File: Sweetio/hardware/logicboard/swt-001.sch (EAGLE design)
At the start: 44 parts, among them IC1 74ACT06N, J1 MKR, J10 THS, J16 MNTR, J2 GPIO, J5 SPI, J6 LED, J7 DIN5, J8 DIN5, J9 DIN5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

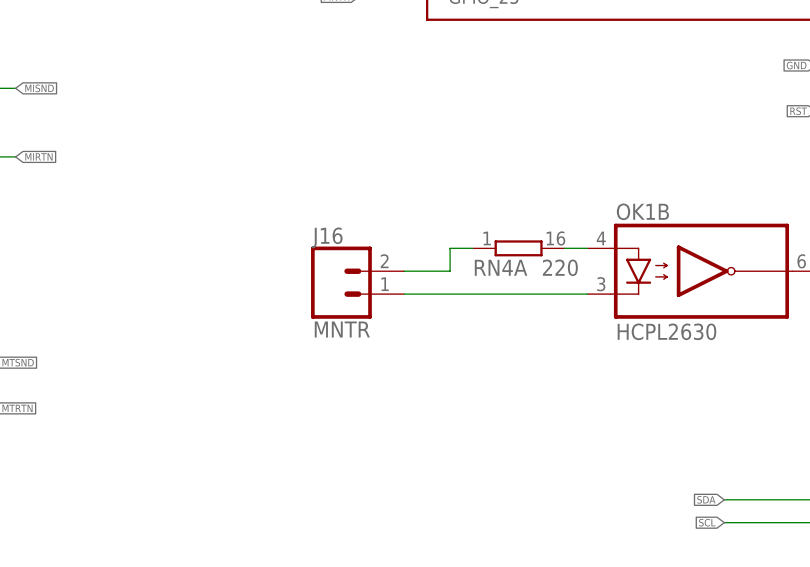
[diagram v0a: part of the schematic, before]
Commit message: Moved JP00.
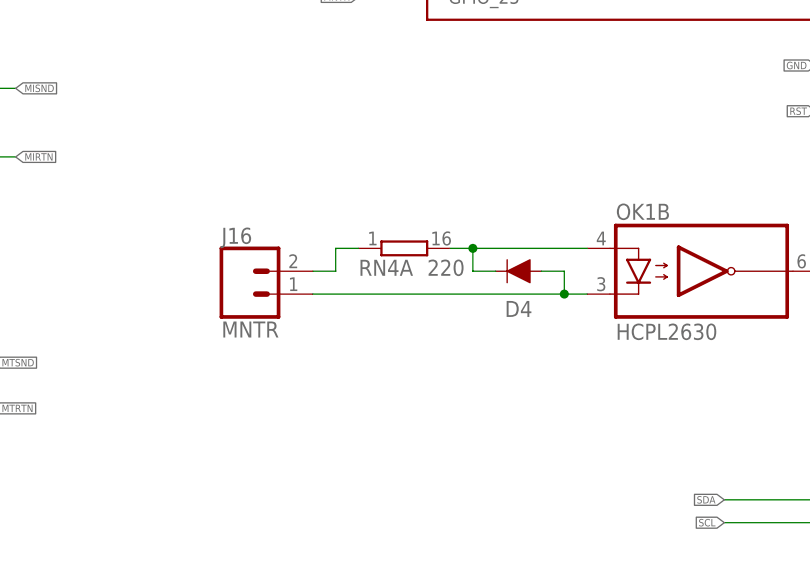
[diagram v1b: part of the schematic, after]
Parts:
- added D4: DIODE-1N4148, SparkFun-DiscreteSemi:DIODE-1N4148
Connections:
- net N$2 renamed BASE
- net N$3 renamed COLLECTOR
- net SND renamed MNTRA
- removed net N$1: OK1B.A2, RN4A.2
- removed net RTN: J16.1, OK1B.C2
- new net MNTRAA: D4.C, OK1B.A2, RN4A.2
- new net MNTRK: D4.A, J16.1, OK1B.C2
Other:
- moved on the sheet: J16, RN4A
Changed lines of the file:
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@@
 <part name="J21" library="Connector" deviceset="TWIG-4P-2.0" device=""/>
 <part name="J22" library="Connector" deviceset="TWIG-4P-2.0" device=""/>
+<part name="D4" library="SparkFun-DiscreteSemi" library_urn="urn:adsk.eagle:library:514" deviceset="DIODE" device="-1N4148" package3d_urn="urn:adsk.eagle:package:38452/1" value=""/>
 </parts>
 <sheets>
@@
 <instance part="NC1" gate="G$1" x="302.26" y="177.8" smashed="yes"/>
 <instance part="NC2" gate="G$1" x="302.26" y="175.26" smashed="yes"/>
-<instance part="RN4" gate="A" x="243.84" y="106.68" smashed="yes">
-<attribute name="VALUE" x="246.38" y="103.632" size="1.778" layer="96"/>
-<attribute name="NAME" x="238.76" y="103.632" size="1.778" layer="95"/>
+<instance part="RN4" gate="A" x="231.14" y="106.68" smashed="yes">
+<attribute name="VALUE" x="233.68" y="103.632" size="1.778" layer="96"/>
+<attribute name="NAME" x="226.06" y="103.632" size="1.778" layer="95"/>
 </instance>
 <instance part="RN4" gate="B" x="177.8" y="124.46" smashed="yes">
@@
 <attribute name="VALUE" x="288.29" y="116.84" size="1.778" layer="96"/>
 </instance>
-<instance part="J16" gate="J1" x="223.52" y="101.6" smashed="yes">
-<attribute name="VALUE" x="220.98" y="96.774" size="1.778" layer="96" font="vector"/>
-<attribute name="NAME" x="220.98" y="107.188" size="1.778" layer="95" font="vector"/>
+<instance part="J16" gate="J1" x="213.36" y="101.6" smashed="yes">
+<attribute name="VALUE" x="210.82" y="96.774" size="1.778" layer="96" font="vector"/>
+<attribute name="NAME" x="210.82" y="107.188" size="1.778" layer="95" font="vector"/>
 </instance>
 <instance part="JP2" gate="J1" x="50.8" y="111.76" smashed="yes">
@@
 <attribute name="NAME" x="77.47" y="86.36" size="1.27" layer="95" rot="R180"/>
 <attribute name="VALUE" x="73.66" y="95.25" size="1.27" layer="96" rot="R270"/>
+</instance>
+<instance part="D4" gate="G$1" x="243.84" y="104.14" smashed="yes" rot="R180">
+<attribute name="NAME" x="243.84" y="99.06" size="1.778" layer="95" align="bottom-center"/>
+<attribute name="VALUE" x="246.38" y="106.172" size="1.778" layer="96" font="vector" rot="R180" align="top-left"/>
 </instance>
 </instances>
@@
 </segment>
 </net>
-<net name="N$1" class="1">
+<net name="MNTRAA" class="1">
 <segment>
 <pinref part="OK1" gate="B" pin="A2"/>
-<wire x1="251.46" y1="106.68" x2="248.92" y2="106.68" width="0.1524" layer="91"/>
+<wire x1="251.46" y1="106.68" x2="238.76" y2="106.68" width="0.1524" layer="91"/>
 <pinref part="RN4" gate="A" pin="2"/>
-</segment>
-</net>
-<net name="RTN" class="1">
+<pinref part="D4" gate="G$1" pin="C"/>
+<wire x1="238.76" y1="106.68" x2="236.22" y2="106.68" width="0.1524" layer="91"/>
+<wire x1="241.3" y1="104.14" x2="238.76" y2="104.14" width="0.1524" layer="91"/>
+<wire x1="238.76" y1="104.14" x2="238.76" y2="106.68" width="0.1524" layer="91"/>
+<junction x="238.76" y="106.68"/>
+</segment>
+</net>
+<net name="MNTRK" class="1">
 <segment>
 <pinref part="OK1" gate="B" pin="C2"/>
-<wire x1="251.46" y1="101.6" x2="231.14" y2="101.6" width="0.1524" layer="91"/>
+<wire x1="251.46" y1="101.6" x2="248.92" y2="101.6" width="0.1524" layer="91"/>
 <pinref part="J16" gate="J1" pin="1"/>
-</segment>
-</net>
-<net name="SND" class="0">
+<pinref part="D4" gate="G$1" pin="A"/>
+<wire x1="248.92" y1="101.6" x2="220.98" y2="101.6" width="0.1524" layer="91"/>
+<wire x1="246.38" y1="104.14" x2="248.92" y2="104.14" width="0.1524" layer="91"/>
+<wire x1="248.92" y1="104.14" x2="248.92" y2="101.6" width="0.1524" layer="91"/>
+<junction x="248.92" y="101.6"/>
+</segment>
+</net>
+<net name="MNTRA" class="0">
 <segment>
 <pinref part="RN4" gate="A" pin="1"/>
-<wire x1="238.76" y1="106.68" x2="236.22" y2="106.68" width="0.1524" layer="91"/>
-<wire x1="236.22" y1="106.68" x2="236.22" y2="104.14" width="0.1524" layer="91"/>
+<wire x1="226.06" y1="106.68" x2="223.52" y2="106.68" width="0.1524" layer="91"/>
+<wire x1="223.52" y1="106.68" x2="223.52" y2="104.14" width="0.1524" layer="91"/>
 <pinref part="J16" gate="J1" pin="2"/>
-<wire x1="236.22" y1="104.14" x2="231.14" y2="104.14" width="0.1524" layer="91"/>
+<wire x1="223.52" y1="104.14" x2="220.98" y2="104.14" width="0.1524" layer="91"/>
 </segment>
 </net>
@@
 </segment>
 </net>
-<net name="N$2" class="0">
+<net name="BASE" class="0">
 <segment>
 <pinref part="T1" gate="G$1" pin="B"/>
@@
 </segment>
 </net>
-<net name="N$3" class="0">
+<net name="COLLECTOR" class="0">
 <segment>
 <pinref part="T1" gate="G$1" pin="C"/>

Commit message: RST switch.
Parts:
- removed JP6: LED, pinhead:PINHD-1X3
- added LED0, LED1: (no value), led:LEDCHIPLED_0603
- added S1: (no value), switch-omron:31-XX
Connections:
- net GND: now also LED0.C, LED1.C, S1.P; no longer JP6.2
- net LED0A: now also LED0.A; no longer JP6.3
- net LED1A: now also LED1.A; no longer JP6.1
- net RST: now also S1.S
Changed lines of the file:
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@@
 <part name="R4" library="resistor" library_urn="urn:adsk.eagle:library:348" deviceset="R-EU_" device="0204/5" package3d_urn="urn:adsk.eagle:package:23488/1" value="1k"/>
 <part name="R5" library="resistor" library_urn="urn:adsk.eagle:library:348" deviceset="R-EU_" device="0204/5" package3d_urn="urn:adsk.eagle:package:23488/1" value="1k"/>
-<part name="JP6" library="pinhead" library_urn="urn:adsk.eagle:library:325" deviceset="PINHD-1X3" device="" package3d_urn="urn:adsk.eagle:package:22458/2" value="LED"/>
 <part name="SUPPLY3" library="supply2" deviceset="GND" device=""/>
 <part name="C6" library="resistor" library_urn="urn:adsk.eagle:library:348" deviceset="C-EU" device="025-024X044" package3d_urn="urn:adsk.eagle:package:23630/1" value="10n"/>
@@
 <part name="J22" library="Connector" deviceset="TWIG-4P-2.0" device=""/>
 <part name="D4" library="SparkFun-DiscreteSemi" library_urn="urn:adsk.eagle:library:514" deviceset="DIODE" device="-1N4148" package3d_urn="urn:adsk.eagle:package:38452/1" value=""/>
+<part name="LED1" library="led" library_urn="urn:adsk.eagle:library:259" deviceset="LED" device="CHIPLED_0603" package3d_urn="urn:adsk.eagle:package:15822/2"/>
+<part name="LED0" library="led" library_urn="urn:adsk.eagle:library:259" deviceset="LED" device="CHIPLED_0603" package3d_urn="urn:adsk.eagle:package:15822/2"/>
+<part name="SUPPLY12" library="supply2" deviceset="GND" device=""/>
+<part name="S1" library="switch-omron" library_urn="urn:adsk.eagle:library:377" deviceset="31-XX" device="" package3d_urn="urn:adsk.eagle:package:27487/1"/>
 </parts>
 <sheets>
@@
 <attribute name="VALUE" x="93.98" y="35.56" size="1.778" layer="96" align="top-center"/>
 </instance>
-<instance part="JP6" gate="A" x="63.5" y="35.56" smashed="yes" rot="MR0">
-<attribute name="NAME" x="69.85" y="41.275" size="1.778" layer="95" rot="MR0"/>
-<attribute name="VALUE" x="69.85" y="27.94" size="1.778" layer="96" rot="MR0"/>
-</instance>
 <instance part="SUPPLY3" gate="GND" x="276.86" y="198.12" smashed="yes"/>
 <instance part="C6" gate="G$1" x="276.86" y="213.36" smashed="yes">
@@
 <attribute name="VALUE" x="246.38" y="106.172" size="1.778" layer="96" font="vector" rot="R180" align="top-left"/>
 </instance>
+<instance part="LED1" gate="G$1" x="68.58" y="38.1" smashed="yes" rot="R270">
+<attribute name="NAME" x="64.008" y="34.544" size="1.778" layer="95"/>
+<attribute name="VALUE" x="64.008" y="32.385" size="1.778" layer="96"/>
+</instance>
+<instance part="LED0" gate="G$1" x="68.58" y="33.02" smashed="yes" rot="R270">
+<attribute name="NAME" x="64.008" y="29.464" size="1.778" layer="95"/>
+<attribute name="VALUE" x="64.008" y="27.305" size="1.778" layer="96"/>
+</instance>
+<instance part="SUPPLY12" gate="GND" x="60.96" y="27.94" smashed="yes"/>
+<instance part="S1" gate="1" x="276.86" y="114.3" smashed="yes" rot="R270">
+<attribute name="NAME" x="274.955" y="120.65" size="1.778" layer="95"/>
+<attribute name="VALUE" x="280.035" y="118.11" size="1.778" layer="96"/>
+</instance>
 </instances>
 <busses>
@@
 <segment>
 <label x="101.6" y="35.56" size="0.8128" layer="95" xref="yes"/>
-<wire x1="66.04" y1="35.56" x2="78.74" y2="35.56" width="0.1524" layer="91"/>
-<pinref part="JP6" gate="A" pin="2"/>
 <pinref part="J6" gate="J$1" pin="2"/>
 <wire x1="78.74" y1="35.56" x2="101.6" y2="35.56" width="0.1524" layer="91"/>
 <wire x1="73.66" y1="20.32" x2="78.74" y2="20.32" width="0.1524" layer="91"/>
 <wire x1="78.74" y1="20.32" x2="78.74" y2="35.56" width="0.1524" layer="91"/>
-<junction x="78.74" y="35.56"/>
 </segment>
 <segment>
@@
 <segment>
 <pinref part="JP00" gate="A" pin="1"/>
-<wire x1="292.1" y1="127" x2="276.86" y2="127" width="0.1524" layer="91"/>
-<label x="276.86" y="127" size="0.8128" layer="95" rot="R180" xref="yes"/>
+<wire x1="292.1" y1="127" x2="269.24" y2="127" width="0.1524" layer="91"/>
+<label x="266.7" y="127" size="0.8128" layer="95" rot="R180" xref="yes"/>
+<wire x1="269.24" y1="127" x2="266.7" y2="127" width="0.1524" layer="91"/>
+<wire x1="269.24" y1="127" x2="269.24" y2="114.3" width="0.1524" layer="91"/>
+<junction x="269.24" y="127"/>
+<pinref part="S1" gate="1" pin="P"/>
+<wire x1="269.24" y1="114.3" x2="271.78" y2="114.3" width="0.1524" layer="91"/>
 </segment>
 <segment>
@@
 <junction x="83.82" y="109.22"/>
 </segment>
+<segment>
+<pinref part="LED1" gate="G$1" pin="C"/>
+<wire x1="63.5" y1="38.1" x2="60.96" y2="38.1" width="0.1524" layer="91"/>
+<wire x1="60.96" y1="38.1" x2="60.96" y2="33.02" width="0.1524" layer="91"/>
+<pinref part="LED0" gate="G$1" pin="C"/>
+<wire x1="60.96" y1="33.02" x2="60.96" y2="30.48" width="0.1524" layer="91"/>
+<wire x1="63.5" y1="33.02" x2="60.96" y2="33.02" width="0.1524" layer="91"/>
+<junction x="60.96" y="33.02"/>
+<pinref part="SUPPLY12" gate="GND" pin="GND"/>
+</segment>
 </net>
 <net name="VCC" class="2">
@@
 <segment>
 <wire x1="292.1" y1="121.92" x2="284.48" y2="121.92" width="0.1524" layer="91"/>
-<label x="276.86" y="121.92" size="0.8128" layer="95" rot="R180" xref="yes"/>
+<label x="266.7" y="121.92" size="0.8128" layer="95" rot="R180" xref="yes"/>
 <pinref part="JP00" gate="A" pin="3"/>
 <pinref part="JP00" gate="A" pin="2"/>
-<wire x1="284.48" y1="121.92" x2="276.86" y2="121.92" width="0.1524" layer="91"/>
+<wire x1="284.48" y1="121.92" x2="266.7" y2="121.92" width="0.1524" layer="91"/>
 <wire x1="292.1" y1="124.46" x2="284.48" y2="124.46" width="0.1524" layer="91"/>
 <wire x1="284.48" y1="124.46" x2="284.48" y2="121.92" width="0.1524" layer="91"/>
 <junction x="284.48" y="121.92"/>
+<pinref part="S1" gate="1" pin="S"/>
+<wire x1="281.94" y1="114.3" x2="284.48" y2="114.3" width="0.1524" layer="91"/>
+<wire x1="284.48" y1="114.3" x2="284.48" y2="121.92" width="0.1524" layer="91"/>
 </segment>
 </net>
@@
 <label x="81.28" y="38.1" size="1.778" layer="95"/>
 <pinref part="R5" gate="G$1" pin="1"/>
-<pinref part="JP6" gate="A" pin="1"/>
 <pinref part="J6" gate="J$1" pin="1"/>
-<wire x1="76.2" y1="38.1" x2="66.04" y2="38.1" width="0.1524" layer="91"/>
 <wire x1="73.66" y1="17.78" x2="76.2" y2="17.78" width="0.1524" layer="91"/>
 <wire x1="76.2" y1="17.78" x2="76.2" y2="38.1" width="0.1524" layer="91"/>
+<pinref part="LED1" gate="G$1" pin="A"/>
+<wire x1="76.2" y1="38.1" x2="71.12" y2="38.1" width="0.1524" layer="91"/>
 <junction x="76.2" y="38.1"/>
 </segment>
@@
 <label x="81.28" y="33.02" size="1.778" layer="95"/>
 <pinref part="R4" gate="G$1" pin="1"/>
-<pinref part="JP6" gate="A" pin="3"/>
 <pinref part="J6" gate="J$1" pin="3"/>
-<wire x1="81.28" y1="33.02" x2="66.04" y2="33.02" width="0.1524" layer="91"/>
 <wire x1="73.66" y1="22.86" x2="81.28" y2="22.86" width="0.1524" layer="91"/>
 <wire x1="81.28" y1="22.86" x2="81.28" y2="33.02" width="0.1524" layer="91"/>
+<pinref part="LED0" gate="G$1" pin="A"/>
+<wire x1="81.28" y1="33.02" x2="71.12" y2="33.02" width="0.1524" layer="91"/>
 <junction x="81.28" y="33.02"/>
 </segment>

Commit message: RST sw.
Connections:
- net RX: now also RN3.4; no longer RN3.3
- net THS: now also RN3.3; no longer RN3.4
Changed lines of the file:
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@@
 <net name="THS" class="0">
-<segment>
-<pinref part="RN3" gate="1" pin="4"/>
-<wire x1="167.64" y1="142.24" x2="170.18" y2="142.24" width="0.1524" layer="91"/>
-<label x="170.18" y="142.24" size="0.8128" layer="95" xref="yes"/>
-</segment>
 <segment>
 <pinref part="SV3" gate="A" pin="6"/>
@@
 <wire x1="228.6" y1="162.56" x2="226.06" y2="162.56" width="0.1524" layer="91"/>
 <label x="226.06" y="162.56" size="0.8128" layer="95" rot="R180" xref="yes"/>
+</segment>
+<segment>
+<pinref part="RN3" gate="1" pin="3"/>
+<wire x1="167.64" y1="147.32" x2="170.18" y2="147.32" width="0.1524" layer="91"/>
+<label x="170.18" y="147.32" size="0.8128" layer="95" xref="yes"/>
 </segment>
 </net>
@@
 </segment>
 <segment>
-<pinref part="RN3" gate="1" pin="3"/>
-<wire x1="167.64" y1="147.32" x2="170.18" y2="147.32" width="0.1524" layer="91"/>
-<label x="170.18" y="147.32" size="0.8128" layer="95" xref="yes"/>
+<pinref part="RN3" gate="1" pin="4"/>
+<wire x1="167.64" y1="142.24" x2="170.18" y2="142.24" width="0.1524" layer="91"/>
+<label x="170.18" y="142.24" size="0.8128" layer="95" xref="yes"/>
 </segment>
 </net>

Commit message: Front Grove conn.
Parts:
- added J23, J24: Grove, Connector:TWIG-4P-2.0
- J20: value (none) -> GPIO
- J21, J22: value (none) -> Grove; device Connector:TWIG-4P-2.0 -> Connector:TWIG-4P-2.0'90D'
- JP2: value (none) -> RTC
- JP8: value (none) -> Extended GPIO
- LED0: value (none) -> Green
- LED1: value (none) -> Red
- S1: value (none) -> RST
- X3: value (none) -> FAN
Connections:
- net GND: now also J23.4, J24.4
- net SCL: now also J23.1, J24.1
- net SDA: now also J23.2, J24.2
- net VDD: now also J23.3, J24.3
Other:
- moved on the sheet: J21, J22, JP2

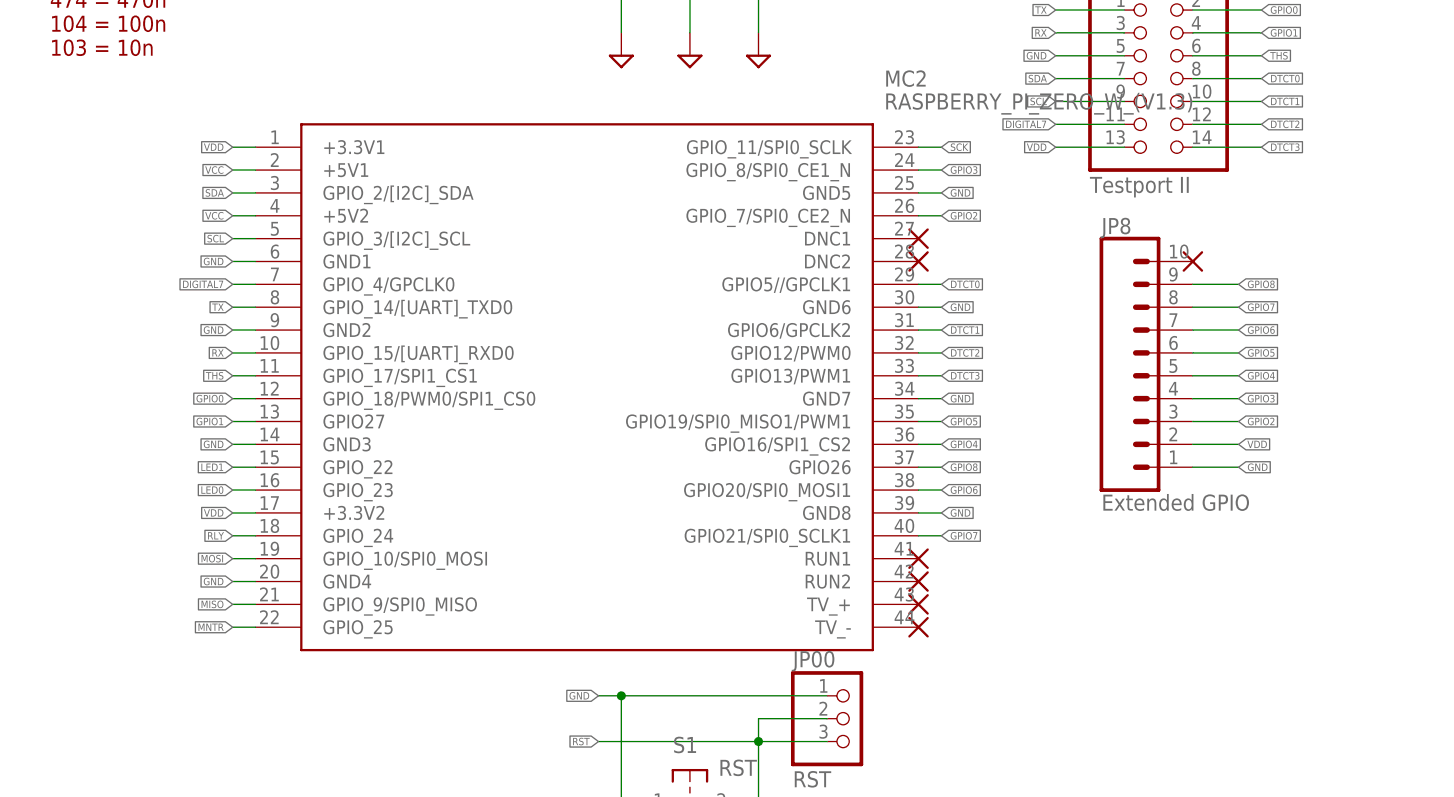
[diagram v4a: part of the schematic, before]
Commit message: Fixed signaling.
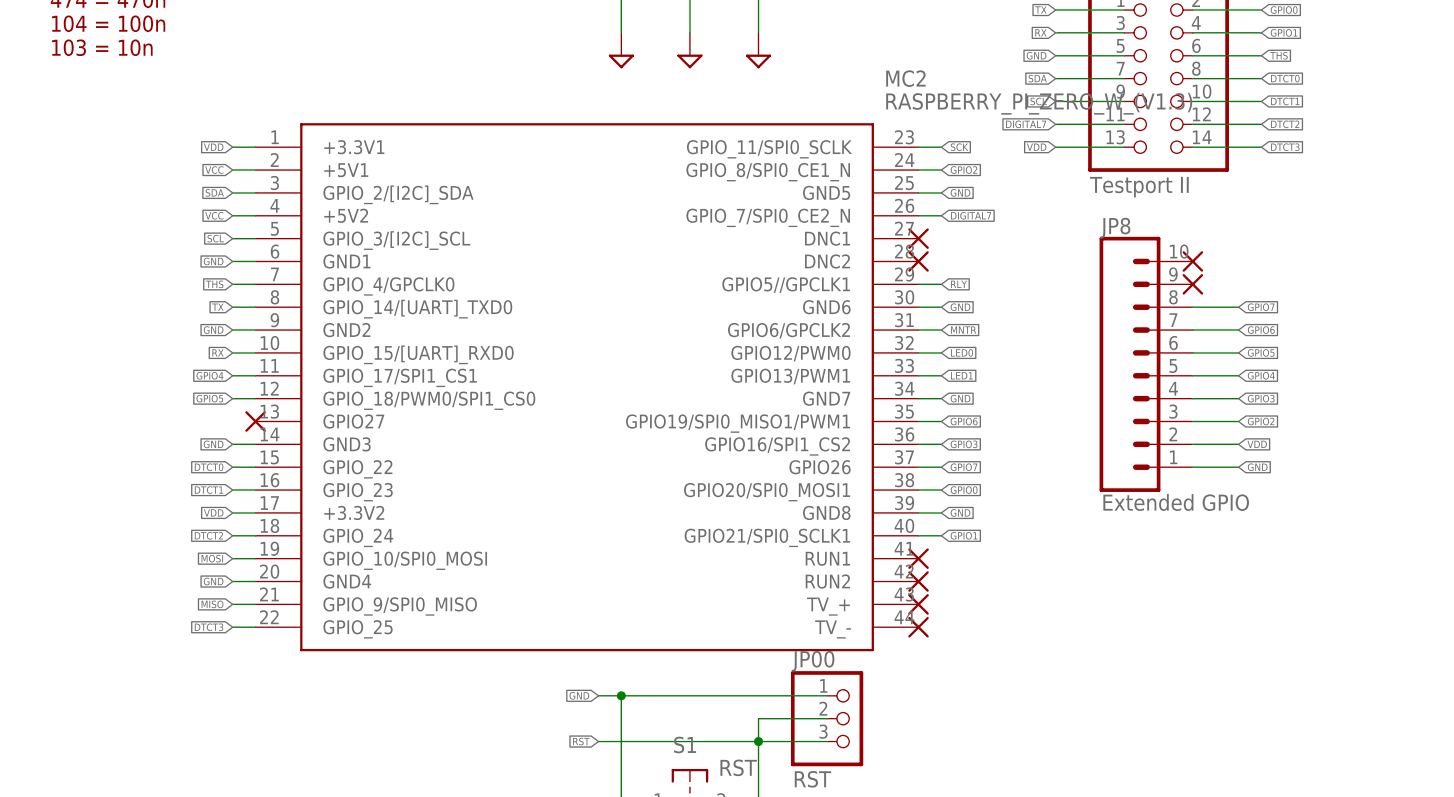
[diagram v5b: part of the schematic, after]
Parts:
- LED0, LED1: device led:LEDCHIPLED_0603 -> led:LEDKA-3528ASYC
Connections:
- removed net GPIO8: JP8.9, MC2.GPIO26
- net DIGITAL7: now also MC2.GPIO_7/SPI0_CE2_N; no longer MC2.GPIO_4/GPCLK0
- net DTCT0: now also MC2.GPIO_22; no longer MC2.GPIO5//GPCLK1
- net DTCT1: now also MC2.GPIO_23; no longer MC2.GPIO6/GPCLK2
- net DTCT2: now also MC2.GPIO_24; no longer MC2.GPIO12/PWM0
- net DTCT3: now also MC2.GPIO_25; no longer MC2.GPIO13/PWM1
- net GPIO0: now also MC2.GPIO20/SPI0_MOSI1; no longer MC2.GPIO_18/PWM0/SPI1_CS0
- net GPIO1: now also MC2.GPIO21/SPI0_SCLK1; no longer MC2.GPIO27
- net GPIO2: now also MC2.GPIO_8/SPI0_CE1_N; no longer MC2.GPIO_7/SPI0_CE2_N
- net GPIO3: now also MC2.GPIO16/SPI1_CS2; no longer MC2.GPIO_8/SPI0_CE1_N
- net GPIO4: now also MC2.GPIO_17/SPI1_CS1; no longer MC2.GPIO16/SPI1_CS2
- net GPIO5: now also MC2.GPIO_18/PWM0/SPI1_CS0; no longer MC2.GPIO19/SPI0_MISO1/PWM1
- net GPIO6: now also MC2.GPIO19/SPI0_MISO1/PWM1; no longer MC2.GPIO20/SPI0_MOSI1
- net GPIO7: now also MC2.GPIO26; no longer MC2.GPIO21/SPI0_SCLK1
- net LED0: now also MC2.GPIO12/PWM0; no longer MC2.GPIO_23
- net LED1: now also MC2.GPIO13/PWM1; no longer MC2.GPIO_22
- net MNTR: now also MC2.GPIO6/GPCLK2; no longer MC2.GPIO_25
- net RLY: now also MC2.GPIO5//GPCLK1; no longer MC2.GPIO_24
- net THS: now also MC2.GPIO_4/GPCLK0; no longer MC2.GPIO_17/SPI1_CS1
